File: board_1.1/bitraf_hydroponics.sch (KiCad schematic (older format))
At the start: 42 parts, among them P1 12V, P10 I2C_4, P11 BUZZER, P12 LDR, P13 TEMP_HUM, P14 PROGRAMMER, P15 SPI, P16 RADIO_433, P2 SWITCH_1, P3 SWITCH_2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

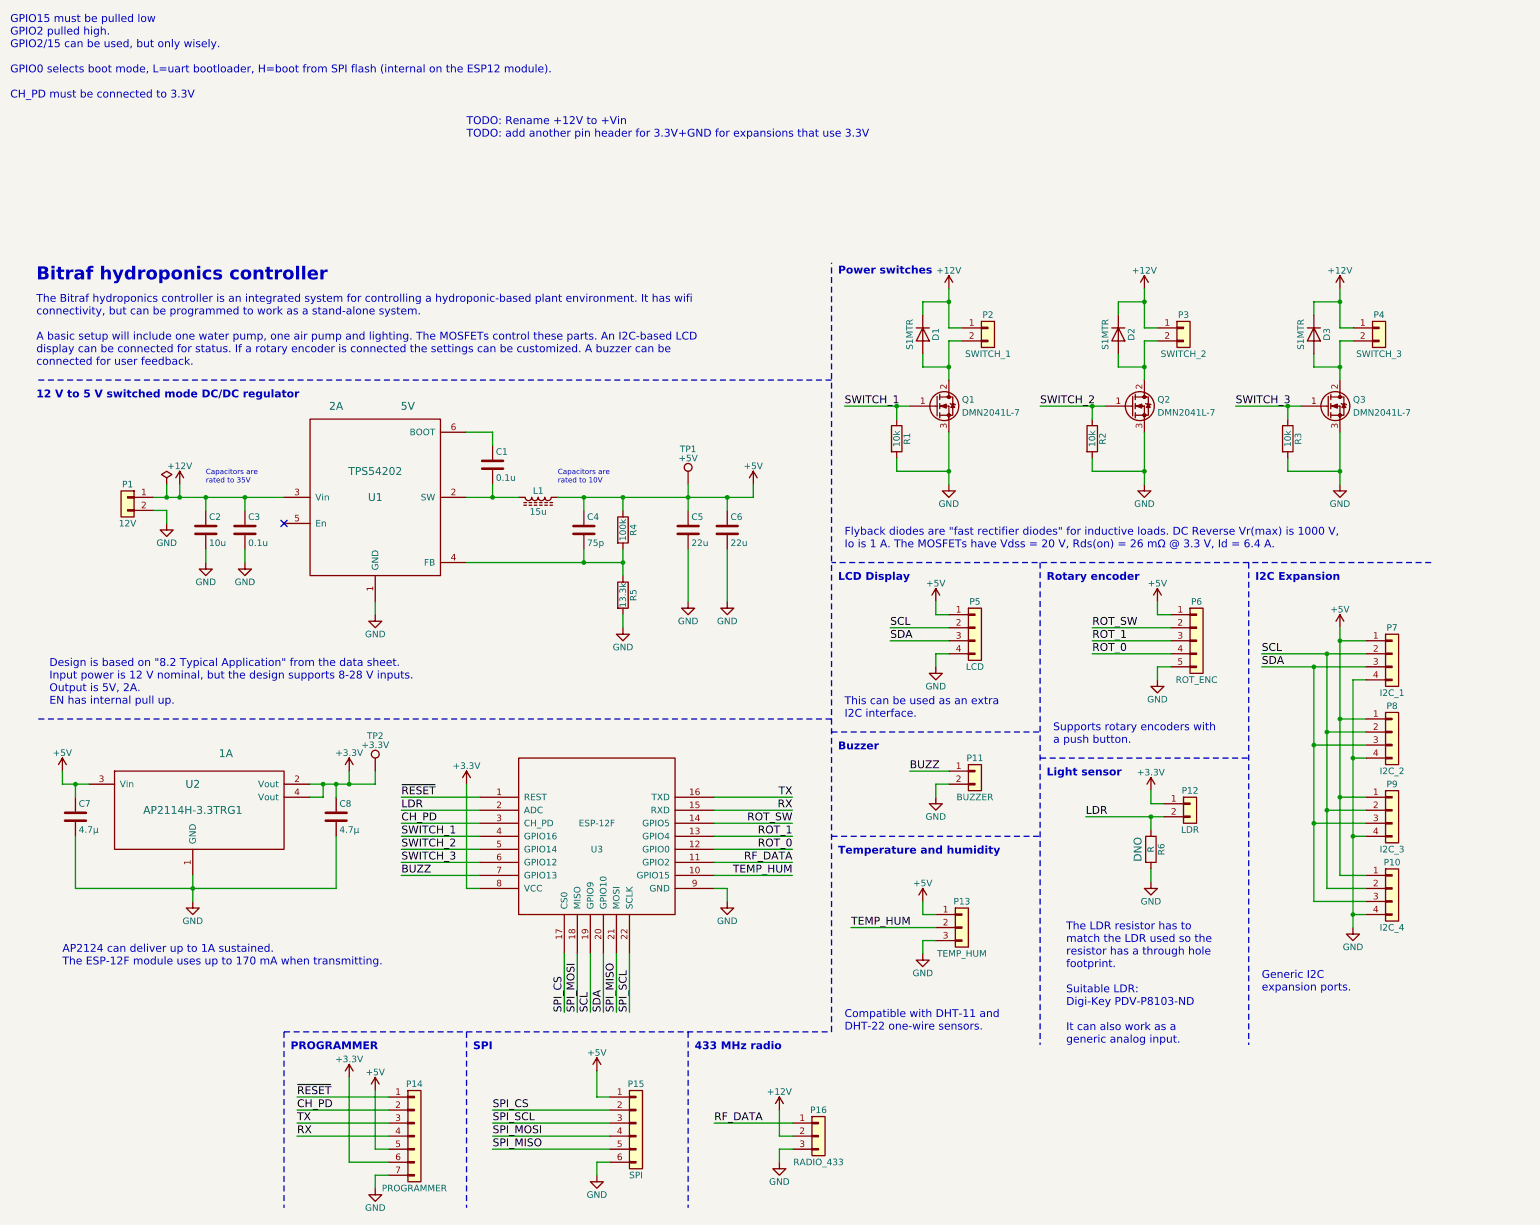
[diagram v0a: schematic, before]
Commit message: added pull-ups and jumper connector for programming
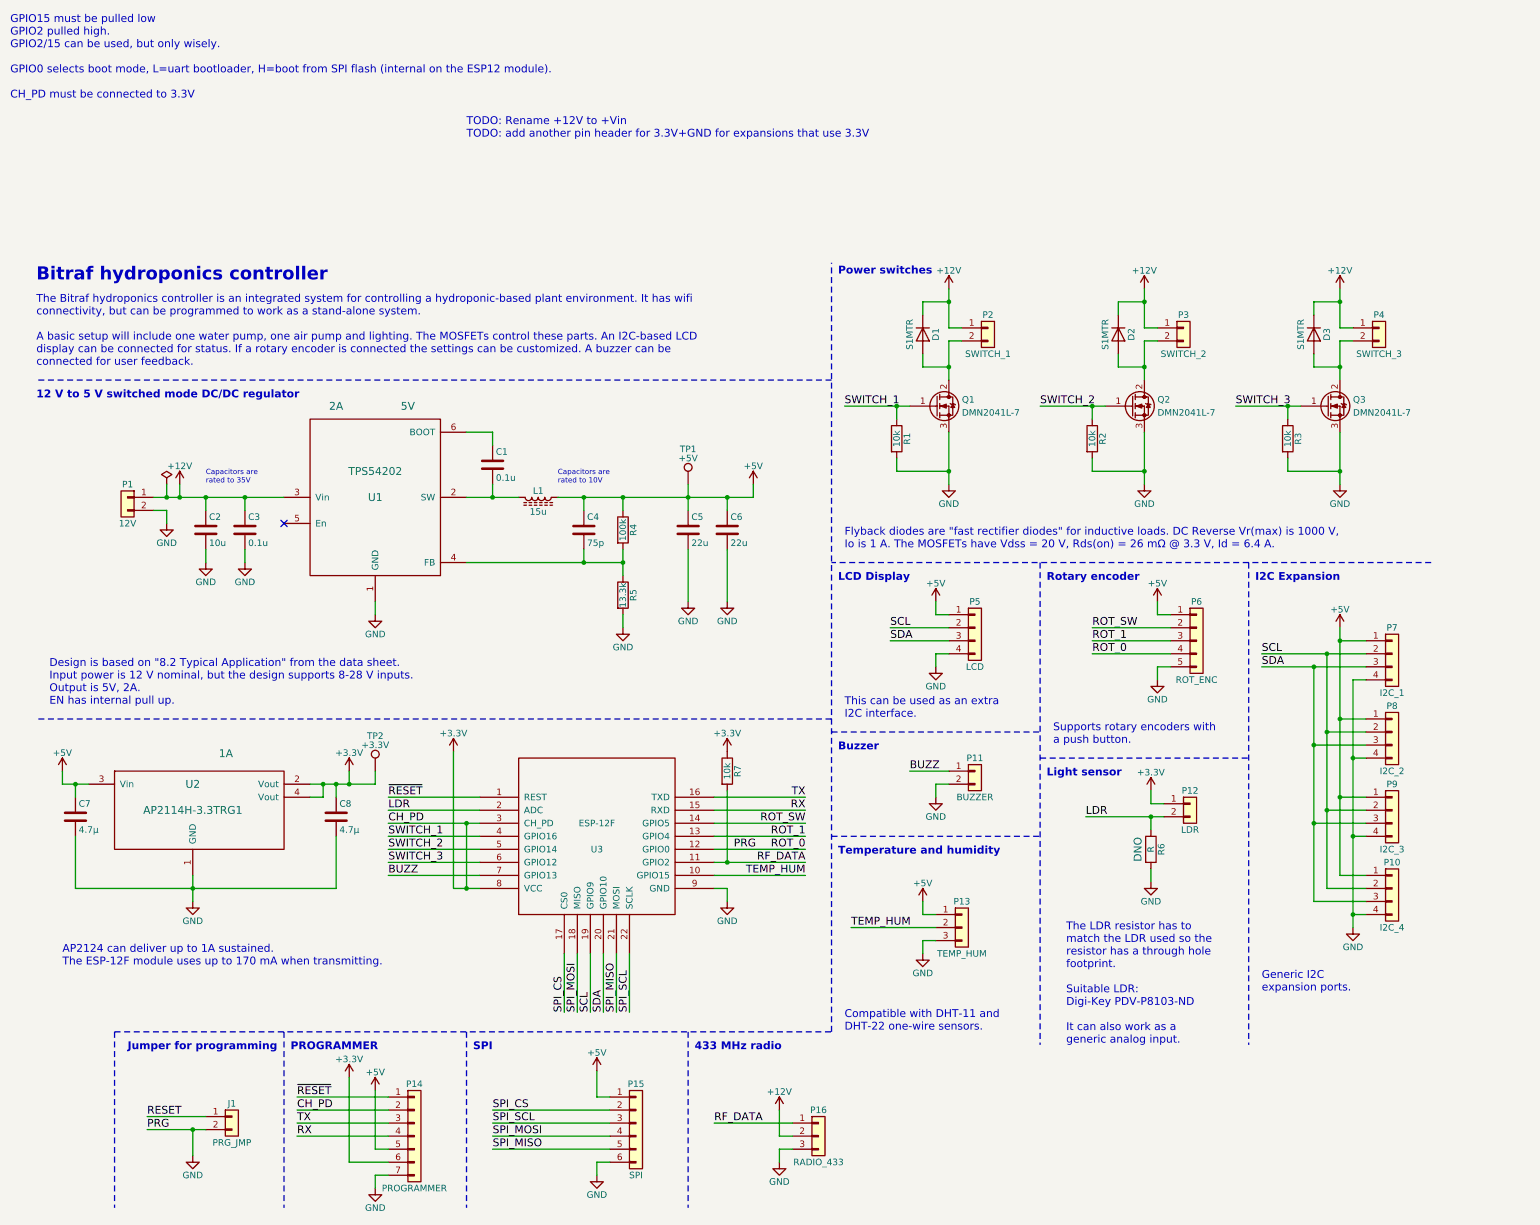
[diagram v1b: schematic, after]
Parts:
- added J1: PRG_JMP, Pin_Headers:Pin_Header_Straight_1x02_Pitch2.54mm, symbol Conn_01x02
- added R7: 10k, Resistors_SMD:R_0805, symbol R
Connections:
- net CH_PD is gone; now on net +3V3: P14.2 (Pin_2), U3.3 (CH_PD)
- net ROT_0 is gone; now on net GND: P6.4 (Pin_4), U3.12 (GPIO0)
- net +3V3: now also R7.1
- net GND: now also J1.2 (Pin_2)
- net RF_DATA: now also R7.2
- new net RESET: J1.1 (Pin_1)
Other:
- note added: "Jumper for programming"

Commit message: fixed faulty pull to GND in the jumper. Added a questions section in the README.md
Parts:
- J1: footprint Pin_Headers:Pin_Header_Straight_1x02_Pitch2.54mm -> Pin_Headers:Pin_Header_Straight_1x03_Pitch2.54mm; symbol Conn_01x02 -> Conn_01x03
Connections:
- net GND: now also J1.3 (Pin_3); no longer J1.2 (Pin_2), P6.4 (Pin_4), U3.12 (GPIO0)
- new net PRG: J1.2 (Pin_2), P6.4 (Pin_4), U3.12 (GPIO0)
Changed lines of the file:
@@
 PRG
 $Comp
-L Conn_01x02 J1
+L Conn_01x03 J1
 U 1 1 5A05A28F
-P 2000 7050
-F 0 "J1" H 2000 7150 50  0000 C CNN
-F 1 "PRG_JMP" H 2000 6850 50  0000 C CNN
-F 2 "Pin_Headers:Pin_Header_Straight_1x02_Pitch2.54mm" H 2000 7050 50  0001 C CNN
-F 3 "" H 2000 7050 50  0001 C CNN
-	1    2000 7050
+P 2000 7000
+F 0 "J1" H 2000 7100 50  0000 C CNN
+F 1 "PRG_JMP" H 2000 6800 50  0000 C CNN
+F 2 "Pin_Headers:Pin_Header_Straight_1x03_Pitch2.54mm" H 2000 7000 50  0001 C CNN
+F 3 "" H 2000 7000 50  0001 C CNN
+	1    2000 7000
 	1    0    0    -1
 $EndComp
-Text Label 1350 7050 0    60   ~ 0
+Text Label 1350 6900 0    60   ~ 0
 RESET
-Text Label 1350 7150 0    60   ~ 0
+Text Label 1350 7000 0    60   ~ 0
 PRG
 Text Notes 1200 6550 0    60   ~ 12
@@
 	7600 1100 7500 1100
 Wire Wire Line
-	7500 1100 7500 1300
-Wire Wire Line
-	7500 1300 7500 1400
+	7500 1100 7500 1400
 Wire Wire Line
 	7500 1000 7600 1000
 Wire Wire Line
-	7500 700  7500 800
-Wire Wire Line
-	7500 800  7500 1000
+	7500 700  7500 1000
 Wire Wire Line
 	7300 1200 7300 1300
@@
 Connection ~ 7500 800
 Wire Wire Line
-	7500 1800 7500 2100
-Wire Wire Line
-	7500 2100 7500 2200
-Wire Wire Line
-	6700 1600 7100 1600
-Wire Wire Line
-	7100 1600 7200 1600
+	7500 1800 7500 2200
+Wire Wire Line
+	6700 1600 7200 1600
 Wire Wire Line
 	7100 1700 7100 1600
@@
 	9100 1100 9000 1100
 Wire Wire Line
-	9000 1100 9000 1300
-Wire Wire Line
-	9000 1300 9000 1400
+	9000 1100 9000 1400
 Wire Wire Line
 	9000 1000 9100 1000
 Wire Wire Line
-	9000 700  9000 800
-Wire Wire Line
-	9000 800  9000 1000
+	9000 700  9000 1000
 Wire Wire Line
 	8800 1200 8800 1300
@@
 Connection ~ 9000 800
 Wire Wire Line
-	9000 1800 9000 2100
-Wire Wire Line
-	9000 2100 9000 2200
-Wire Wire Line
-	8200 1600 8600 1600
-Wire Wire Line
-	8600 1600 8700 1600
+	9000 1800 9000 2200
+Wire Wire Line
+	8200 1600 8700 1600
 Wire Wire Line
 	8600 1700 8600 1600
@@
 	10600 1100 10500 1100
 Wire Wire Line
-	10500 1100 10500 1300
-Wire Wire Line
-	10500 1300 10500 1400
+	10500 1100 10500 1400
 Wire Wire Line
 	10500 1000 10600 1000
 Wire Wire Line
-	10500 700  10500 800
-Wire Wire Line
-	10500 800  10500 1000
+	10500 700  10500 1000
 Wire Wire Line
 	10300 1200 10300 1300
@@
 	10300 900  10300 800
 Wire Wire Line
-	10500 1800 10500 2100
-Wire Wire Line
-	10500 2100 10500 2200
-Wire Wire Line
-	9700 1600 10100 1600
-Wire Wire Line
-	10100 1600 10200 1600
+	10500 1800 10500 2200
+Wire Wire Line
+	9700 1600 10200 1600
 Wire Wire Line
 	10100 1700 10100 1600
@@
 	9200 3500 8600 3500
 Wire Wire Line
-	1400 2300 1500 2300
-Wire Wire Line
-	1500 2300 1600 2300
-Wire Wire Line
-	1600 2300 1800 2300
-Wire Wire Line
-	1800 2300 2100 2300
-Wire Wire Line
-	2100 2300 2400 2300
+	1400 2300 2400 2300
 Wire Wire Line
 	1600 2300 1600 2200
@@
 	7500 4400 7200 4400
 Wire Wire Line
-	8550 4750 9050 4750
-Wire Wire Line
-	9050 4750 9150 4750
+	8550 4750 9150 4750
 Wire Wire Line
 	9050 4750 9050 4850
@@
 	10400 5300 10700 5300
 Wire Wire Line
-	10500 3300 10500 3400
-Wire Wire Line
-	10500 3400 10500 4000
-Wire Wire Line
-	10500 4000 10500 4600
-Wire Wire Line
-	10500 4600 10500 5200
+	10500 3300 10500 5200
 Wire Wire Line
 	10600 5500 10700 5500
@@
 	10400 4100 10700 4100
 Wire Wire Line
-	9900 3600 10300 3600
-Wire Wire Line
-	10300 3600 10700 3600
-Wire Wire Line
-	9900 3500 10400 3500
-Wire Wire Line
-	10400 3500 10700 3500
+	9900 3600 10700 3600
+Wire Wire Line
+	9900 3500 10700 3500
 Wire Wire Line
 	10500 3400 10700 3400
@@
 	8800 1300 9000 1300
 Wire Wire Line
-	3800 2300 4000 2300
-Wire Wire Line
-	4000 2300 4200 2300
-Wire Wire Line
-	4500 2300 4700 2300
-Wire Wire Line
-	4700 2300 5000 2300
-Wire Wire Line
-	5000 2300 5500 2300
-Wire Wire Line
-	5500 2300 5800 2300
-Wire Wire Line
-	5800 2300 6000 2300
+	3800 2300 4200 2300
+Wire Wire Line
+	4500 2300 6000 2300
 Wire Wire Line
 	5000 3200 5000 3300
@@
 Connection ~ 4000 2300
 Wire Wire Line
-	5500 2200 5500 2300
-Wire Wire Line
-	5500 2300 5500 2400
+	5500 2200 5500 2400
 Connection ~ 5500 2300
 Wire Wire Line
@@
 	5500 3100 5500 2700
 Wire Wire Line
-	10400 3500 10400 4100
-Wire Wire Line
-	10400 4100 10400 4700
-Wire Wire Line
-	10400 4700 10400 5300
+	10400 3500 10400 5300
 Connection ~ 10400 4100
 Connection ~ 10400 3500
 Connection ~ 10400 4700
 Wire Wire Line
-	10300 3600 10300 4200
-Wire Wire Line
-	10300 4200 10300 4800
-Wire Wire Line
-	10300 4800 10300 5400
+	10300 3600 10300 5400
 Connection ~ 10300 4800
 Connection ~ 10300 4200
@@
 	10600 3700 10700 3700
 Wire Wire Line
-	10600 3700 10600 4300
-Wire Wire Line
-	10600 4300 10600 4900
-Wire Wire Line
-	10600 4900 10600 5500
-Wire Wire Line
-	10600 5500 10600 5600
+	10600 3700 10600 5600
 Wire Notes Line
 	11200 2800 6600 2800
@@
 	8200 2800 8200 6500
 Wire Wire Line
-	5700 5100 5800 5100
-Wire Wire Line
-	5800 5100 6400 5100
+	5700 5100 6400 5100
 Wire Notes Line
 	8200 4300 9800 4300
@@
 	3800 6400 3800 7750
 Wire Wire Line
-	5000 2700 5000 2800
-Wire Wire Line
-	5000 2800 5000 2900
-Wire Wire Line
-	3800 2800 4700 2800
-Wire Wire Line
-	4700 2800 5000 2800
+	5000 2700 5000 2900
+Wire Wire Line
+	3800 2800 5000 2800
 Wire Wire Line
 	4700 2800 4700 2700
@@
 	5800 5300 5800 5400
 Wire Wire Line
-	3700 5300 3800 5300
-Wire Wire Line
-	3800 5300 3900 5300
+	3700 5300 3900 5300
 Wire Wire Line
 	3700 5300 3700 4250
@@
 	700  4400 700  4500
 Wire Wire Line
-	700  4500 800  4500
-Wire Wire Line
-	800  4500 900  4500
-Wire Wire Line
-	2600 4500 2700 4500
-Wire Wire Line
-	2700 4500 2800 4500
-Wire Wire Line
-	2800 4500 2900 4500
-Wire Wire Line
-	2900 4500 3100 4500
+	700  4500 900  4500
+Wire Wire Line
+	2600 4500 3100 4500
 Wire Wire Line
 	2900 4500 2900 4400
@@
 Connection ~ 2700 4500
 Wire Wire Line
-	1700 5200 1700 5300
-Wire Wire Line
-	1700 5300 1700 5400
+	1700 5200 1700 5400
 Wire Wire Line
 	800  4500 800  4600
@@
 	800  4900 800  5300
 Wire Wire Line
-	800  5300 1700 5300
-Wire Wire Line
-	1700 5300 2800 5300
+	800  5300 2800 5300
 Connection ~ 1700 5300
 Wire Wire Line
@@
 	6400 4600 5700 4600
 Wire Wire Line
-	3200 4800 3800 4800
-Wire Wire Line
-	3800 4800 3900 4800
+	3200 4800 3900 4800
 Wire Wire Line
 	3200 4600 3900 4600
@@
 Connection ~ 5800 5100
 Wire Wire Line
-	1800 7050 1350 7050
-Wire Wire Line
-	1800 7150 1700 7150
-Wire Wire Line
-	1700 7150 1350 7150
+	1800 7000 1350 7000
 Wire Notes Line
 	1100 6400 1100 7750
@@
 	5800 5100 5800 4550
 Wire Wire Line
-	1700 7150 1700 7350
-Connection ~ 1700 7150
+	1700 7100 1700 7250
 $Comp
-L GND #PWR?
+L GND #PWR041
 U 1 1 5A05DB47
-P 1700 7350
-F 0 "#PWR?" H 1700 7100 50  0001 C CNN
-F 1 "GND" H 1700 7200 50  0000 C CNN
-F 2 "" H 1700 7350 50  0001 C CNN
-F 3 "" H 1700 7350 50  0001 C CNN
-	1    1700 7350
+P 1700 7250
+F 0 "#PWR041" H 1700 7000 50  0001 C CNN
+F 1 "GND" H 1700 7100 50  0000 C CNN
+F 2 "" H 1700 7250 50  0001 C CNN
+F 3 "" H 1700 7250 50  0001 C CNN
+	1    1700 7250
 	1    0    0    -1
 $EndComp
+Wire Wire Line
+	1800 6900 1350 6900
+Wire Wire Line
+	1700 7100 1800 7100
 $EndSCHEMATC
